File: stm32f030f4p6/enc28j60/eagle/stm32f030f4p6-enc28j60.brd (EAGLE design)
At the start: 68.6 x 53.4 mm, 29 parts, among them IC2 LM1117IDTX-3.3, IC3 LP2950, X1 MINI-USB-UX60-MB-5ST

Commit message: updated stm32f030f4p6/enc28j60/eagle
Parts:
- added BOOT-SW: (no value), pinhead:1X03
- added R1: 5K, resistor:0204/5
- moved VDD{,A} 0.63 mm to (55.9, 25.8)
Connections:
- net N$1 renamed VDDA
- net N$10 renamed PA3
- net N$11 renamed PA4@L
- net N$12 renamed PA5
- net N$13 renamed PA6
- net N$14 renamed PF1@LED
- net N$187 renamed 5V@EXT
- net N$188 renamed 3V3@EXT
- net N$19 renamed PF1@OCC
- net N$190 renamed PA7
- net N$20 renamed PF0@OCC
- net N$21 renamed RESET
- net N$23 renamed PA4@R
- net N$29 renamed PF0@LED
- net N$4 renamed PF0
- net N$5 renamed PF1
- net N$6 renamed PA4
- net N$7 renamed PA0
- net N$8 renamed PA1
- net N$9 renamed PA2
- removed net N$3: STM32F030F4PX_L.1, STM32F030F4PX_L.2
- new net BOOT: R1.1, STM32F030F4PX_L.1, STM32F030F4PX_L.2
- new net N$1: BOOT-SW.2, R1.2
- net GND@0: now also BOOT-SW.1
- net VDD: now also BOOT-SW.3
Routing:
- net BOOT: track 0.00 -> 21.4 mm
- net GND@0: track 234.2 -> 252.9 mm
- net VDD: track 172.1 -> 178.9 mm
- net N$3: track 2.54 -> 0.00 mm
- net N$1: track 0.00 -> 2.54 mm
- net VDDA: track 11.4 -> 13.5 mm
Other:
- board text added: "stm32f030f4px protoboard v0.4; contact@embed.shop"
- board text removed: "stm32f030f4px protoboard v0.3; contact@embed.shop"

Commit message: fixed 473b0256177802d8c32fc4b0b20f1561cfde31d8
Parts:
- moved R1 12.7 mm to (43.5, 20.0)
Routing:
- net N$1: track 2.54 -> 19.7 mm
- net BOOT: track 21.4 -> 4.79 mm
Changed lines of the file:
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@@
 <description language="de">&lt;b&gt;EAGLE Design Rules&lt;/b&gt;
 &lt;p&gt;
-Die Standard-Design-Rules sind so gewählt, dass sie für
+Die Standard-Design-Rules sind so gewÃ¤hlt, dass sie fÃ¼r
 die meisten Anwendungen passen. Sollte ihre Platine
 besondere Anforderungen haben, treffen Sie die erforderlichen
@@
 <autorouter>
 <pass name="Default">
-<param name="RoutingGrid" value="50mil"/>
+<param name="RoutingGrid" value="12.5mil"/>
 <param name="AutoGrid" value="1"/>
-<param name="Efforts" value="0"/>
+<param name="Efforts" value="1"/>
 <param name="TopRouterVariant" value="1"/>
 <param name="tpViaShape" value="round"/>
-<param name="PrefDir.1" value="a"/>
+<param name="PrefDir.1" value="-"/>
 <param name="PrefDir.2" value="0"/>
 <param name="PrefDir.3" value="0"/>
@@
 <param name="PrefDir.14" value="0"/>
 <param name="PrefDir.15" value="0"/>
-<param name="PrefDir.16" value="a"/>
+<param name="PrefDir.16" value="|"/>
 <param name="cfVia" value="8"/>
 <param name="cfNonPref" value="5"/>
@@
 <element name="LED1_R1" library="resistor" package="0204/7" value="" x="2.032" y="42.164" rot="R90"/>
 <element name="BOOT-SW" library="pinhead" package="1X03" value="" x="58.42" y="20.32" rot="R180"/>
-<element name="R1" library="resistor" package="0204/5" value="5K" x="55.88" y="22.86" rot="MR180"/>
+<element name="R1" library="resistor" package="0204/5" value="5K" x="43.4975" y="20.0025" rot="MR180"/>
 </elements>
 <signals>
@@
 <wire x1="40.64" y1="17.78" x2="40.64" y2="15.24" width="1.27" layer="16"/>
 <contactref element="R1" pad="1"/>
-<wire x1="53.34" y1="22.86" x2="52.07" y2="21.59" width="0.254" layer="1"/>
-<wire x1="52.07" y1="21.59" x2="52.07" y2="17.145" width="0.254" layer="1"/>
-<wire x1="52.07" y1="17.145" x2="51.435" y2="16.51" width="0.254" layer="1"/>
-<wire x1="51.435" y1="16.51" x2="41.275" y2="16.51" width="0.254" layer="1"/>
-<wire x1="41.275" y1="16.51" x2="40.64" y2="17.145" width="0.254" layer="1"/>
-<wire x1="40.64" y1="17.145" x2="40.64" y2="17.78" width="0.254" layer="1"/>
+<wire x1="40.9575" y1="20.0025" x2="40.64" y2="17.78" width="0.254" layer="16"/>
 </signal>
 <signal name="PF0">
@@
 <wire x1="45.72" y1="17.78" x2="45.72" y2="15.24" width="1.27" layer="16"/>
 <contactref element="LED1_JP" pad="2"/>
-<wire x1="45.72" y1="17.78" x2="45.72" y2="20.32" width="1.27" layer="16"/>
-<wire x1="45.72" y1="20.32" x2="44.45" y2="21.59" width="0.6096" layer="16"/>
-<wire x1="44.45" y1="21.59" x2="44.45" y2="22.86" width="0.6096" layer="16"/>
+<wire x1="45.72" y1="17.78" x2="44.45" y2="19.05" width="0.6096" layer="16"/>
+<wire x1="44.45" y1="19.05" x2="44.45" y2="22.86" width="0.6096" layer="16"/>
 </signal>
 <signal name="PA0">
@@
 <via x="38.1" y="30.48" extent="1-16" drill="0.9" shape="square"/>
 </signal>
-<signal name="N$144">
-<via x="53.34" y="20.32" extent="1-16" drill="0.9" shape="square"/>
-<via x="48.26" y="20.32" extent="1-16" drill="0.9" shape="square"/>
-<wire x1="48.26" y1="20.32" x2="53.34" y2="20.32" width="0" layer="19" extent="1-1"/>
-</signal>
 <signal name="N$148">
 <via x="60.96" y="22.86" extent="1-16" drill="0.9" shape="square"/>
+<via x="58.42" y="22.86" extent="1-16" drill="0.9" shape="square"/>
+<wire x1="58.42" y1="22.86" x2="60.96" y2="22.86" width="0" layer="19" extent="1-1"/>
 </signal>
 <signal name="N$153">
@@
 <via x="35.56" y="35.56" extent="1-16" drill="1.1" shape="square"/>
 </signal>
+<signal name="N$3">
+<via x="35.56" y="38.1" extent="1-16" drill="1.1" shape="square"/>
+</signal>
 <signal name="N$46">
-<via x="35.56" y="38.1" extent="1-16" drill="1.1" shape="square"/>
 <via x="38.1" y="38.1" extent="1-16" drill="1.1" shape="square"/>
-<wire x1="35.56" y1="38.1" x2="38.1" y2="38.1" width="0" layer="19" extent="1-1"/>
 </signal>
 <signal name="N$47">
@@
 <via x="55.88" y="30.48" extent="1-16" drill="0.9" shape="square"/>
 </signal>
+<signal name="N$4">
+<via x="60.325" y="38.735" extent="1-16" drill="0.5" shape="square"/>
+</signal>
+<signal name="N$5">
+<via x="38.1" y="36.195" extent="1-16" drill="0.5" shape="square"/>
+</signal>
 <signal name="N$215">
-<via x="38.1" y="36.195" extent="1-16" drill="0.5" shape="square"/>
-<via x="60.325" y="38.735" extent="1-16" drill="0.5" shape="square"/>
 <via x="40.005" y="27.94" extent="1-16" drill="0.5" shape="square"/>
 <via x="40.005" y="25.7175" extent="1-16" drill="0.5" shape="square"/>
+<wire x1="40.005" y1="25.7175" x2="40.005" y2="27.94" width="0" layer="19" extent="1-1"/>
 </signal>
 <signal name="N$216">
@@
 <signal name="N$237">
 <via x="2.54" y="10.16" extent="1-16" drill="0.5" shape="square"/>
-</signal>
-<signal name="N$238">
-<via x="40.64" y="20.32" extent="1-16" drill="0.9" shape="square"/>
 </signal>
 <signal name="N$239">
@@
 <contactref element="R1" pad="2"/>
 <contactref element="BOOT-SW" pad="2"/>
-<wire x1="58.42" y1="20.32" x2="58.42" y2="22.86" width="1.27" layer="1"/>
+<wire x1="46.0375" y1="20.0025" x2="46.99" y2="20.0025" width="0.4064" layer="1"/>
+<wire x1="46.99" y1="20.0025" x2="46.99" y2="16.51" width="0.4064" layer="1"/>
+<wire x1="46.99" y1="16.51" x2="57.15" y2="16.51" width="0.4064" layer="1"/>
+<wire x1="57.15" y1="16.51" x2="57.15" y2="20.32" width="0.4064" layer="1"/>
+<wire x1="57.15" y1="20.32" x2="58.42" y2="20.32" width="0.4064" layer="1"/>
 </signal>
 </signals>

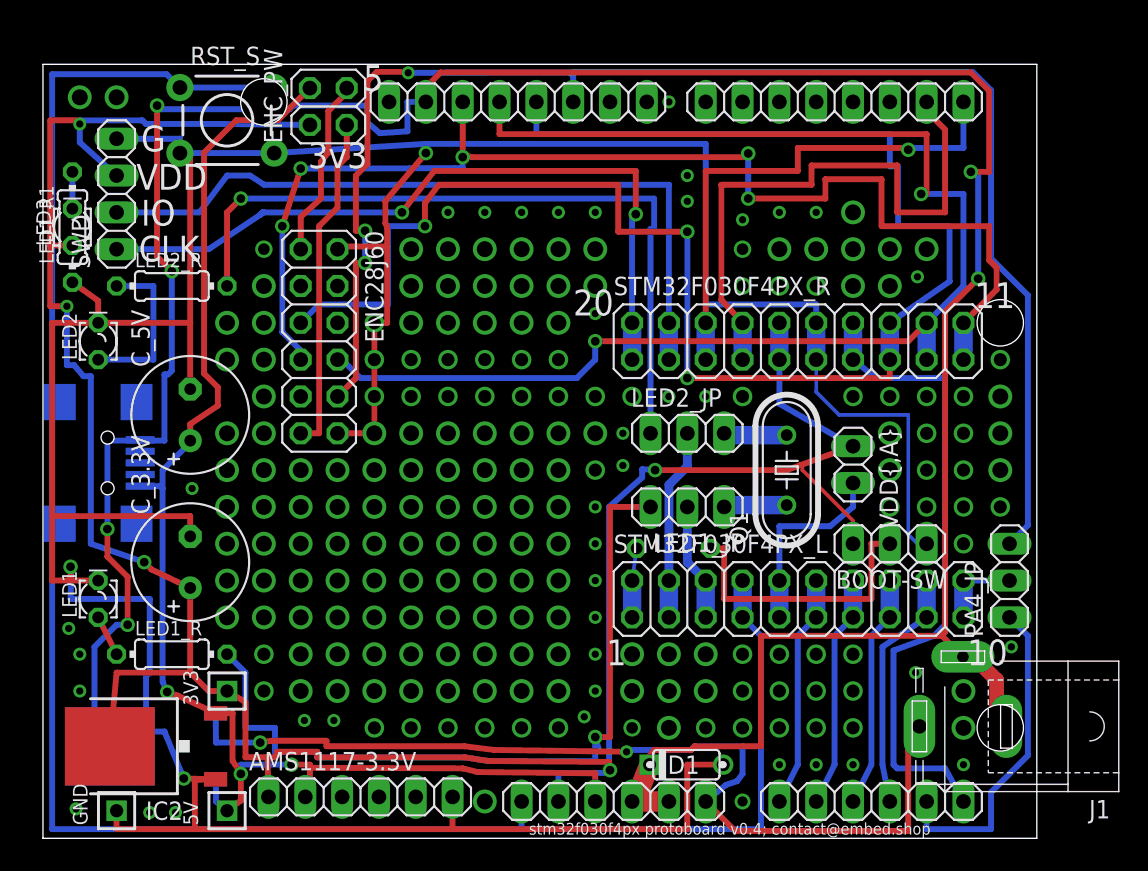
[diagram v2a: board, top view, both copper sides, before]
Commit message: Updated stm32f030f4p6/enc28j60/eagle
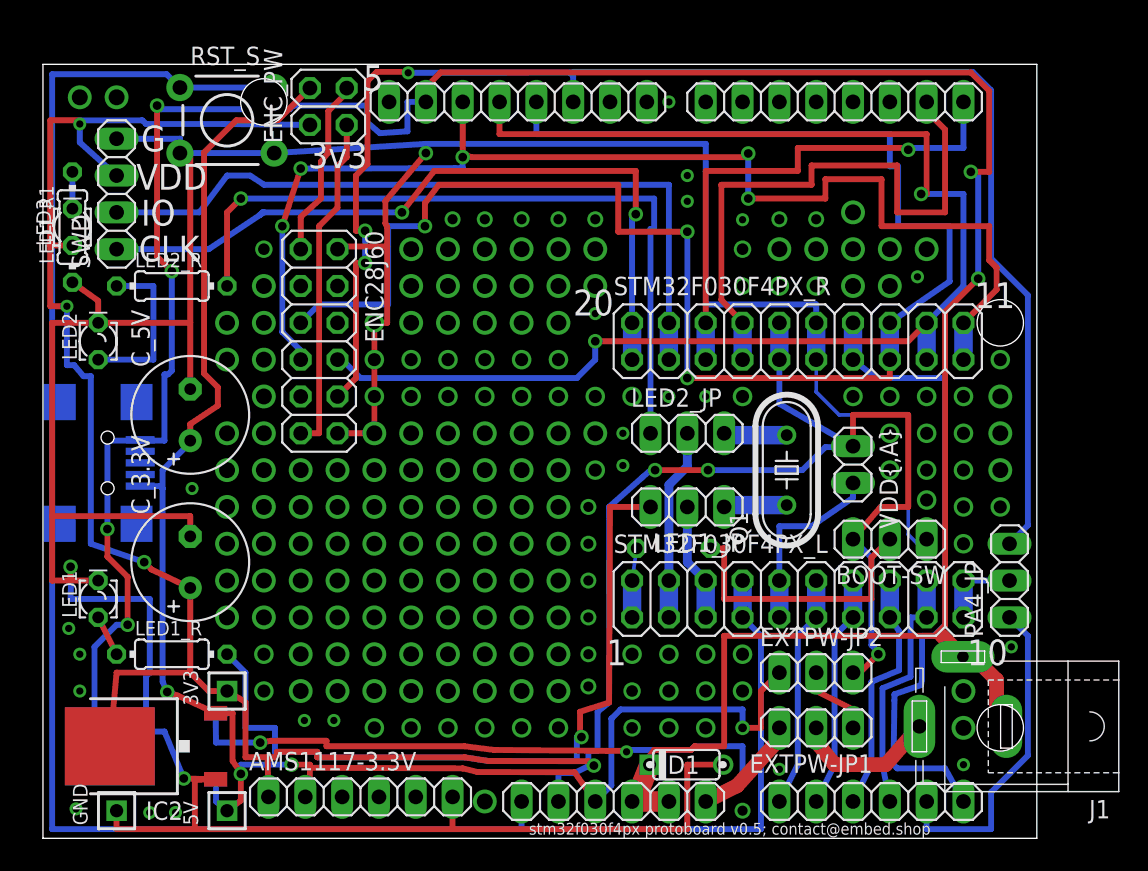
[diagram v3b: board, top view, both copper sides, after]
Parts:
- added EXTPW-JP1, EXTPW-JP2: (no value), pinhead:1X03
- moved BOOT-SW 0.32 mm to (58.4, 20.6)
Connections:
- net N$1 renamed BOOT@R
- removed net N$24: IC1.6, IC3.1, J1.3
- new net VIN: EXTPW-JP1.2, J1.3
- new net VIN@HIGH: EXTPW-JP1.3, IC1.6, IC3.1
- new net VIN@LOW: EXTPW-JP1.1, EXTPW-JP2.2
- net 5V: now also EXTPW-JP2.1
- net VDD: now also EXTPW-JP2.3
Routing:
- net N$24: track 66.5 -> 0.00 mm, vias 2 -> 0
- net VIN@HIGH: track 0.00 -> 51.9 mm, vias 0 -> 2
- net 5V: track 94.6 -> 116.0 mm, vias 3 -> 4
- net VDD: track 178.9 -> 197.9 mm, vias 5 -> 7
- net VIN: track 0.00 -> 10.0 mm
- net VIN@LOW: track 0.00 -> 5.38 mm
- net PF1@LED: track 54.0 -> 52.8 mm
- net PA2: track 16.1 -> 17.0 mm
- net PA3: track 16.9 -> 17.7 mm
- net VDDA: track 13.5 -> 13.0 mm
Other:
- board text added: "stm32f030f4px protoboard v0.5; contact@embed.shop"
- board text removed: "stm32f030f4px protoboard v0.4; contact@embed.shop"

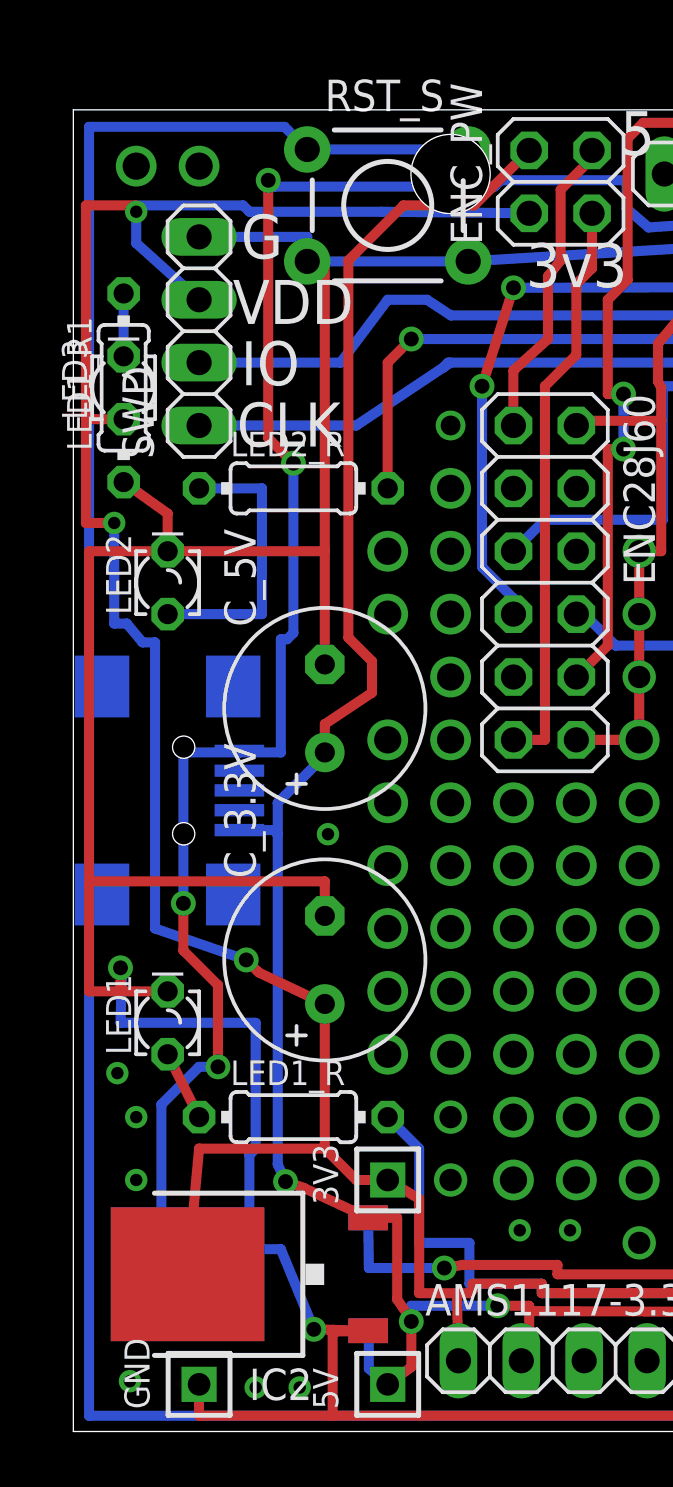
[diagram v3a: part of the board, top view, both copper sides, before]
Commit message: Connected enc28j60 RST in stm32f030f4p6/enc28j60/eagle
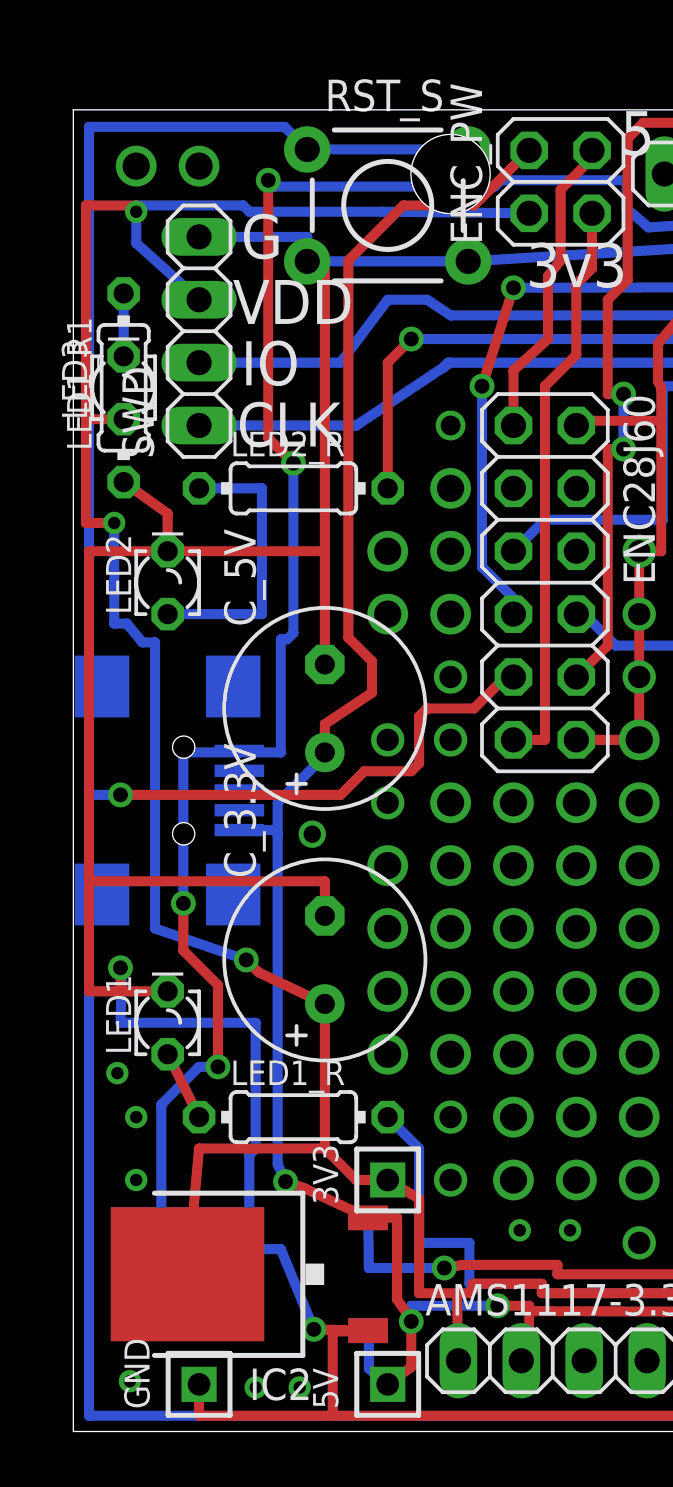
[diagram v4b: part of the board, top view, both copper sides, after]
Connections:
- net RESET: now also ENC28J60.9
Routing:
- net RESET: track 136.2 -> 156.5 mm, vias 0 -> 1
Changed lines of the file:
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@@
 <wire x1="49.53" y1="0.635" x2="49.53" y2="13.97" width="0.4064" layer="16"/>
 <wire x1="49.53" y1="13.97" x2="48.26" y2="15.24" width="0.4064" layer="16"/>
-<wire x1="0.635" y1="0.635" x2="0.635" y2="52.705" width="0.4064" layer="16"/>
+<wire x1="0.635" y1="0.635" x2="0.635" y2="25.7175" width="0.4064" layer="16"/>
+<contactref element="ENC28J60" pad="9"/>
+<wire x1="0.635" y1="25.7175" x2="0.635" y2="52.705" width="0.4064" layer="16"/>
+<wire x1="17.78" y1="30.48" x2="17.4625" y2="30.48" width="0.4064" layer="1"/>
+<wire x1="17.4625" y1="30.48" x2="16.1925" y2="29.21" width="0.4064" layer="1"/>
+<wire x1="16.1925" y1="29.21" x2="14.2875" y2="29.21" width="0.4064" layer="1"/>
+<wire x1="14.2875" y1="29.21" x2="13.97" y2="28.8925" width="0.4064" layer="1"/>
+<wire x1="13.97" y1="28.8925" x2="13.97" y2="26.9875" width="0.4064" layer="1"/>
+<wire x1="13.97" y1="26.9875" x2="13.6525" y2="26.67" width="0.4064" layer="1"/>
+<wire x1="13.6525" y1="26.67" x2="11.7475" y2="26.67" width="0.4064" layer="1"/>
+<wire x1="11.7475" y1="26.67" x2="10.795" y2="25.7175" width="0.4064" layer="1"/>
+<wire x1="10.795" y1="25.7175" x2="1.905" y2="25.7175" width="0.4064" layer="1"/>
+<via x="1.905" y="25.7175" extent="1-16" drill="0.6" shape="square"/>
+<wire x1="1.905" y1="25.7175" x2="0.635" y2="25.7175" width="0.4064" layer="16"/>
 </signal>
 <signal name="GND@0">
@@
 </signal>
 <signal name="N$140">
-<via x="15.24" y="30.48" extent="1-16" drill="1.1" shape="square"/>
+<via x="15.24" y="30.48" extent="1-16" drill="0.9" shape="square"/>
 </signal>
 <signal name="N$141">
-<via x="15.24" y="27.94" extent="1-16" drill="1.1" shape="square"/>
+<via x="15.24" y="27.94" extent="1-16" drill="0.9" shape="square"/>
 </signal>
 <signal name="N$142">
@@
 </signal>
 <signal name="N$163">
-<via x="12.7" y="25.4" extent="1-16" drill="1.1" shape="square"/>
+<via x="12.7" y="25.4" extent="1-16" drill="0.9" shape="square"/>
 </signal>
 <signal name="N$164">
@@
 </signal>
 <signal name="N$168">
-<via x="12.7" y="27.94" extent="1-16" drill="1.1" shape="square"/>
+<via x="12.7" y="27.94" extent="1-16" drill="0.9" shape="square"/>
 </signal>
 <signal name="N$172">
@@
 </signal>
 <signal name="N$233">
-<via x="10.287" y="24.13" extent="1-16" drill="0.5" shape="square"/>
+<via x="9.652" y="24.13" extent="1-16" drill="0.7" shape="square"/>
 </signal>
 <signal name="N$234">
